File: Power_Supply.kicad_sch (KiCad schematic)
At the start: 14 parts, among them U1 R-783.3-1.0, U2 R-785.0-1.0

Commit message: Тестовая версия
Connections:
- net E1 renamed E3
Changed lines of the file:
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@@
     (stroke (width 0) (type default) (color 0 0 0 0))
   )
-  (global_label "E1" (shape input) (at 90.932 69.088 0) (fields_autoplaced)
+  (global_label "E3" (shape input) (at 90.932 69.088 0) (fields_autoplaced)
     (effects (font (size 1.27 1.27)) (justify left))
     (property "Intersheet References" "${INTERSHEET_REFS}" (id 0) (at 95.7037 69.0086 0)

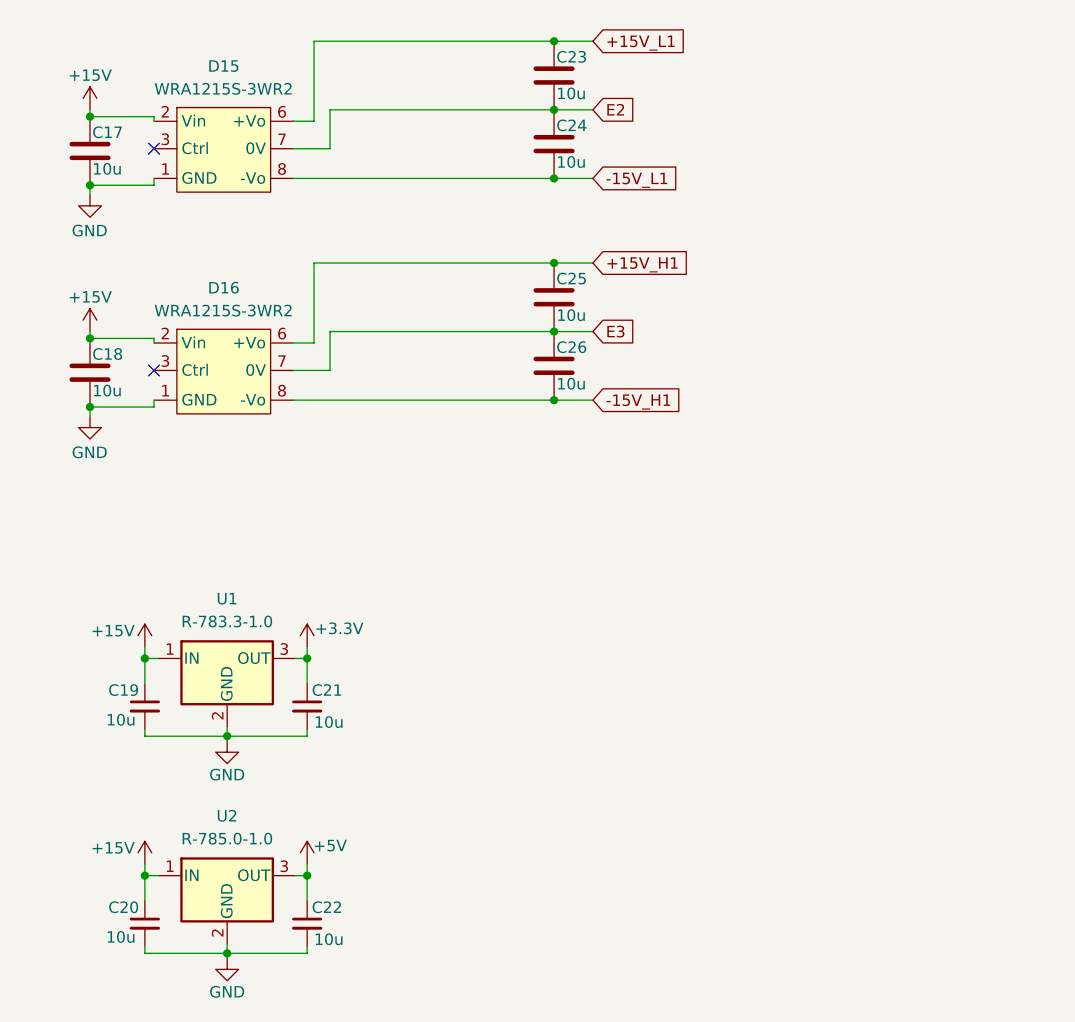
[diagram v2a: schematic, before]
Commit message: Убрал питание 3.3В
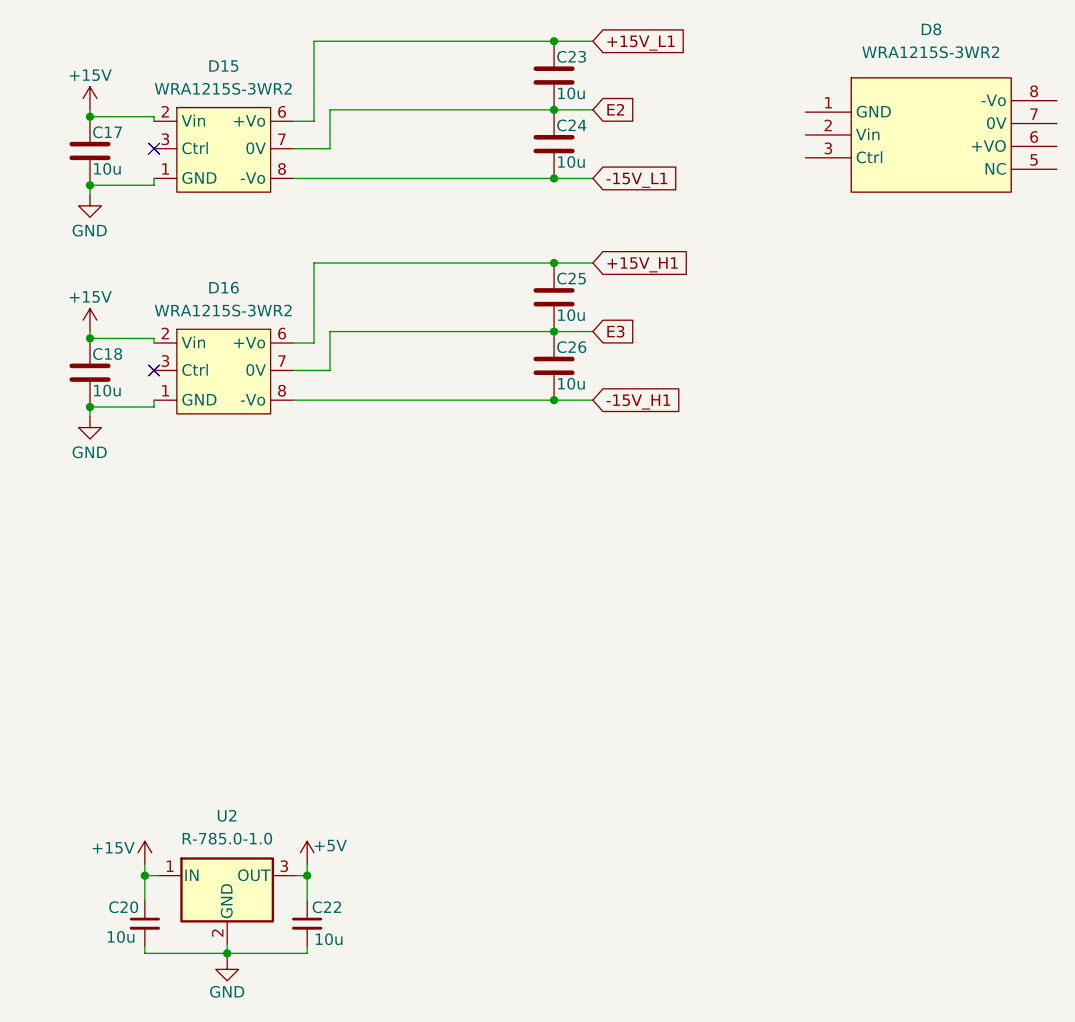
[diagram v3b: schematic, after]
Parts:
- removed C19, C21: 10u, Capacitor_SMD:C_1210_3225Metric_Pad1.33x2.70mm_HandSolder, symbol Device:C_Small
- removed U1: R-783.3-1.0, Converter_DCDC:Converter_DCDC_RECOM_R-78E-0.5_THT, symbol Regulator_Switching:R-783.3-1.0
- added D8: WRA1215S-3WR2, symbol Mornsun:WRA_S-3WR2

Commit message: Развел все дорожки
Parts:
- removed D15, D16: WRA1215S-3WR2, Mornsun:WRA1215S-3WR2, symbol Morsun:WRA1215S-3WR2
- removed U2: R-785.0-1.0, Converter_DCDC:Converter_DCDC_RECOM_R-78E-0.5_THT, symbol Regulator_Switching:R-783.3-1.0
- added D11: WRA1215S-3WR2, Mornsun:WRA_S-3WR2, symbol Mornsun:WRA_S-3WR2
- added D12: K78xxM-1000R3, Mornsun:K78xx-1000R3, symbol Mornsun:K78xxM-1000R3 ÕýÊä³ö
- D8: footprint (none) -> Mornsun:WRA_S-3WR2
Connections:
- net +15V_L1 is gone; now on net -15V_L: C23.1
- net -15V_L1 is gone; now on net +15V_L: C24.2
- net +15V: now also D8.2 (Vin), D11.2 (Vin), D12.1 (Vin)
- net +5V: now also D12.3 (+Vo)
- net E2: now also D8.7 (0V)
- net E3: now also D11.7 (0V)
- net GND: now also D8.1 (GND), D11.1 (GND), D12.2 (GND)
- net +15V_L: now reaches D8.6 (+VO)
- net -15V_L: now reaches D8.8 (-Vo)
- net +15V_H1 renamed -15V_H
- net -15V_H: now also D11.8 (-Vo)
- net -15V_H1 renamed +15V_H
- net +15V_H: now also D11.6 (+VO)
- no-connect marks 2 -> 4
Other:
- moved on the sheet: C17, C18, C20, C22, C23, C24, C25, C26

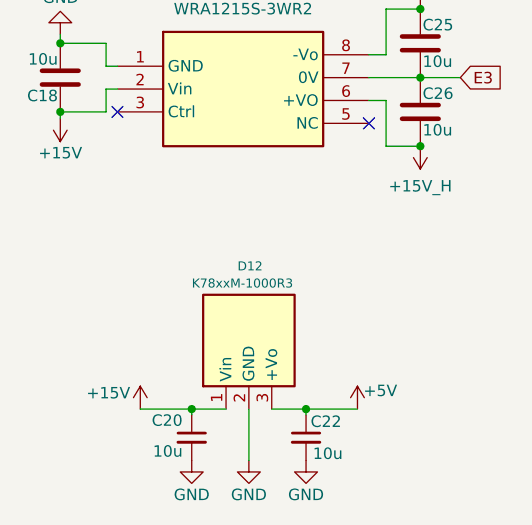
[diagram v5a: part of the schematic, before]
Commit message: Изменения: изменил BOM, сделал заказ
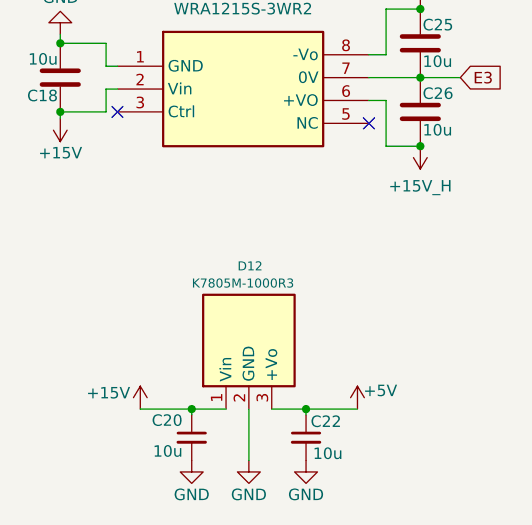
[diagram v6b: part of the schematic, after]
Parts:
- D12: value K78xxM-1000R3 -> K7805M-1000R3
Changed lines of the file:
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@@
 			)
 		)
-		(property "Value" "K78xxM-1000R3"
+		(property "Value" "K7805M-1000R3"
 			(at 46.355 118.745 90)
 			(effects

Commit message: VER2.1: внес все исправления для заказа в Китае
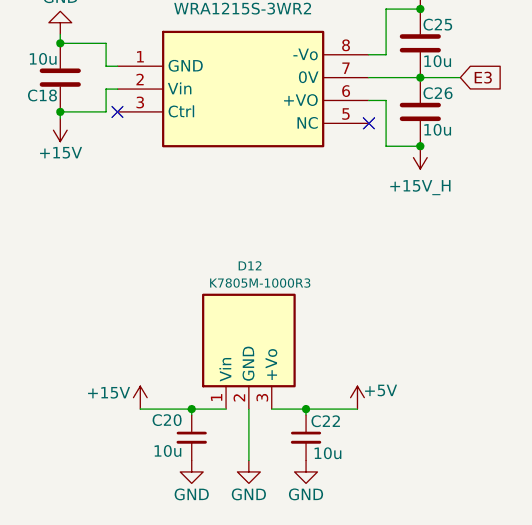
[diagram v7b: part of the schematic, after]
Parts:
- D12: footprint Mornsun:K78xx-1000R3 -> Mornsun:K78xxM-1000R3
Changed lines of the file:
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@@
 		)
 		(property "Value" "K7805M-1000R3"
-			(at 46.355 118.745 90)
+			(at 48.26 118.745 90)
 			(effects
 				(font
@@
 			)
 		)
-		(property "Footprint" "Mornsun:K78xx-1000R3"
+		(property "Footprint" "Mornsun:K78xxM-1000R3"
 			(at 59.309 125.857 0)
 			(effects
